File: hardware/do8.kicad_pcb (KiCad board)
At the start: 4 copper layers, 100 x 85 mm, 116 parts, among them J101 TNG-Power-TOP, J102 TNG-Power-BTM, J103 TNG-Data-TOP, J104 TNG-Data-BTM, P102 Debug, P103 PE, P201 OUTPUT0, P202 OUTPUT1, P203 OUTPUT2, P204 OUTPUT3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

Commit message: change value
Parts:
- C208: value 2.2uF/50V -> 4.7uF/50V

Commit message: specify tbd
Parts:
- C115: value TBD -> 2.2uF
- C127, C128: value 4.7nF/2kV -> 1nF/2kV
- R101: value 510 -> 1k
- RP201: value 200 -> 180
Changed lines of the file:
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@@
   (page A4)
   (layers
-    (0 F.Cu signal)
+    (0 F.Cu signal hide)
     (1 GND power hide)
     (2 VCC power hide)
@@
     (aux_axis_origin 89.8 62.5)
     (grid_origin 89.8 62.5)
-    (visible_elements FFFFFF7F)
+    (visible_elements FFFF7F7F)
     (pcbplotparams
       (layerselection 0x010fc_ffffffff)
@@
       (effects (font (size 0.29972 0.29972) (thickness 0.07493)))
     )
-    (fp_text value 200 (at 1.01 -0.02 90) (layer F.Fab)
+    (fp_text value 180 (at 1.01 -0.02 90) (layer F.Fab)
       (effects (font (size 0.29972 0.29972) (thickness 0.07493)))
     )
@@
       (effects (font (size 0.2 0.2) (thickness 0.05)) (justify mirror))
     )
-    (fp_text value TBD (at 0.05 0.375 180) (layer B.Fab)
+    (fp_text value 2.2uF (at 0.05 0.375 180) (layer B.Fab)
       (effects (font (size 0.2 0.2) (thickness 0.05)) (justify mirror))
     )
@@
       (effects (font (size 0.2 0.2) (thickness 0.05)))
     )
-    (fp_text value 510 (at 0 -0.15 90) (layer F.Fab)
+    (fp_text value 1k (at 0 -0.15 90) (layer F.Fab)
       (effects (font (size 0.2 0.2) (thickness 0.05)))
     )
@@
       (effects (font (size 0.3 0.3) (thickness 0.075)))
     )
-    (fp_text value 4.7nF/2kV (at 0 -0.65) (layer F.Fab)
+    (fp_text value 1nF/2kV (at 0 -0.65) (layer F.Fab)
       (effects (font (size 0.3 0.3) (thickness 0.075)))
     )
@@
       (effects (font (size 0.3 0.3) (thickness 0.075)))
     )
-    (fp_text value 4.7nF/2kV (at 0 -0.65) (layer F.Fab)
+    (fp_text value 1nF/2kV (at 0 -0.65) (layer F.Fab)
       (effects (font (size 0.3 0.3) (thickness 0.075)))
     )

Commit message: fix diodes
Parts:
- D201, D202, D203, D204, D205, D206, D207, D208: value SMBJ24A -> SMBJ24CA
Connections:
- J101 pad 21: (no net) -> Net-(J101-Pad21)
- J101 pad 22: (no net) -> Net-(J101-Pad22)
- J101 pad 23: (no net) -> Net-(J101-Pad23)
- J101 pad 24: (no net) -> Net-(J101-Pad24)
- J101 pad 25: (no net) -> Net-(J101-Pad25)
- J101 pad 26: (no net) -> Net-(J101-Pad26)
- J101 pad 27: (no net) -> Net-(J101-Pad27)
- J101 pad 28: (no net) -> Net-(J101-Pad28)
- J101 pad 29: (no net) -> Net-(J101-Pad29)
- J101 pad 30: (no net) -> Net-(J101-Pad30)
- J102 pad 21: (no net) -> Net-(J102-Pad21)
- J102 pad 22: (no net) -> Net-(J102-Pad22)
- J102 pad 23: (no net) -> Net-(J102-Pad23)
- J102 pad 24: (no net) -> Net-(J102-Pad24)
- J102 pad 25: (no net) -> Net-(J102-Pad25)
- J102 pad 26: (no net) -> Net-(J102-Pad26)
- J102 pad 27: (no net) -> Net-(J102-Pad27)
- J102 pad 28: (no net) -> Net-(J102-Pad28)
- J102 pad 29: (no net) -> Net-(J102-Pad29)
- J102 pad 30: (no net) -> Net-(J102-Pad30)
- J103 pad 35: (no net) -> Net-(J103-Pad35)
- J103 pad 37: (no net) -> Net-(J103-Pad37)
- U101 pad 11: (no net) -> Net-(U101-Pad11)
- U101 pad 17: (no net) -> Net-(U101-Pad17)
- U101 pad 2: (no net) -> Net-(U101-Pad2)
- U101 pad 21: (no net) -> Net-(U101-Pad21)
- U101 pad 22: (no net) -> Net-(U101-Pad22)
- U101 pad 26: (no net) -> Net-(U101-Pad26)
- U101 pad 27: (no net) -> Net-(U101-Pad27)
- U101 pad 28: (no net) -> Net-(U101-Pad28)
- U101 pad 3: (no net) -> Net-(U101-Pad3)
- U101 pad 4: (no net) -> Net-(U101-Pad4)
- U101 pad 43: (no net) -> Net-(U101-Pad43)
- U101 pad 46: (no net) -> Net-(U101-Pad46)
- U101 pad 7: (no net) -> Net-(U101-Pad7)
- U104 pad 7: (no net) -> Net-(U104-Pad7)
- U104 pad 8: (no net) -> Net-(U104-Pad8)
- U106 pad 12: (no net) -> Net-(U106-Pad12)
- U106 pad 2: (no net) -> Net-(U106-Pad2)
- U201 pad 2: (no net) -> Net-(U201-Pad2)
- U201 pad 26: (no net) -> Net-(U201-Pad26)
- U201 pad 27: (no net) -> Net-(U201-Pad27)
- U201 pad 28: (no net) -> Net-(U201-Pad28)
- U201 pad 29: (no net) -> Net-(U201-Pad29)
- U201 pad 30: (no net) -> Net-(U201-Pad30)

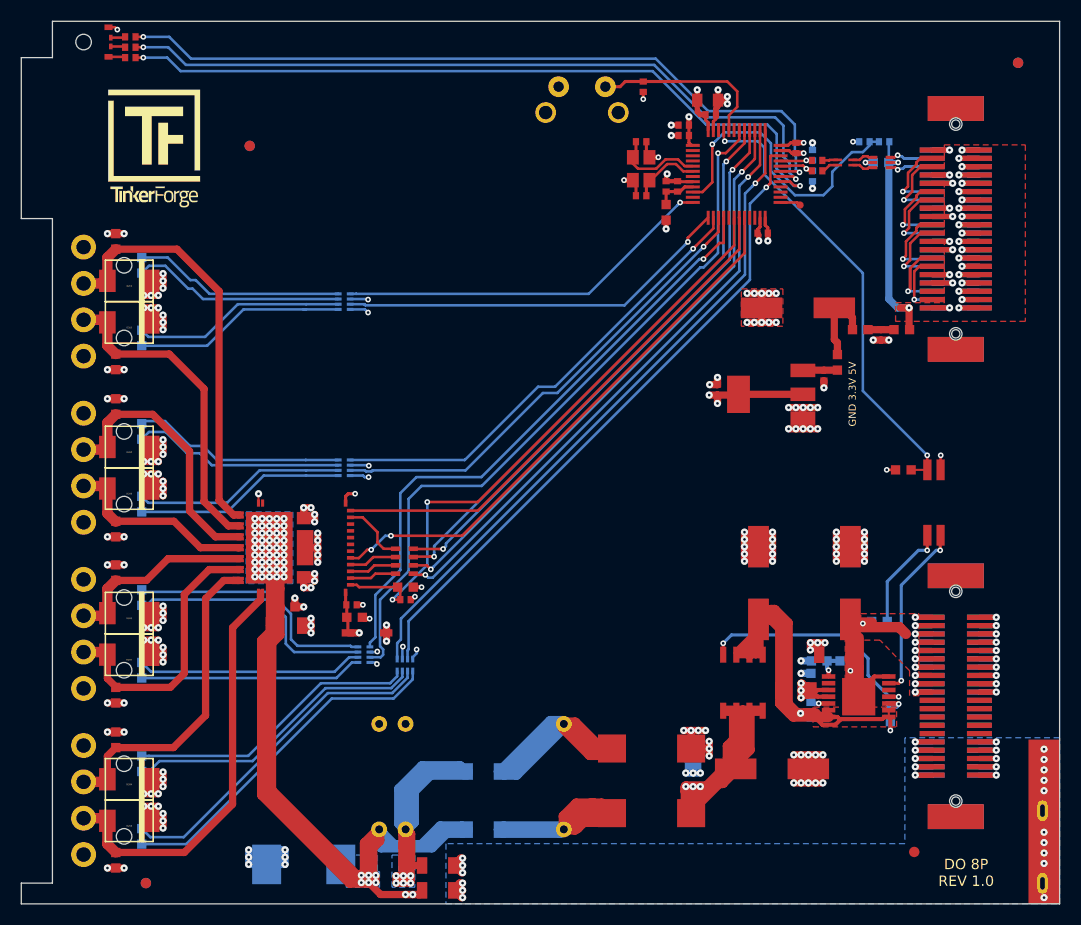
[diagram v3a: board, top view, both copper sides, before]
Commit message: version 1.1.
fix footprints
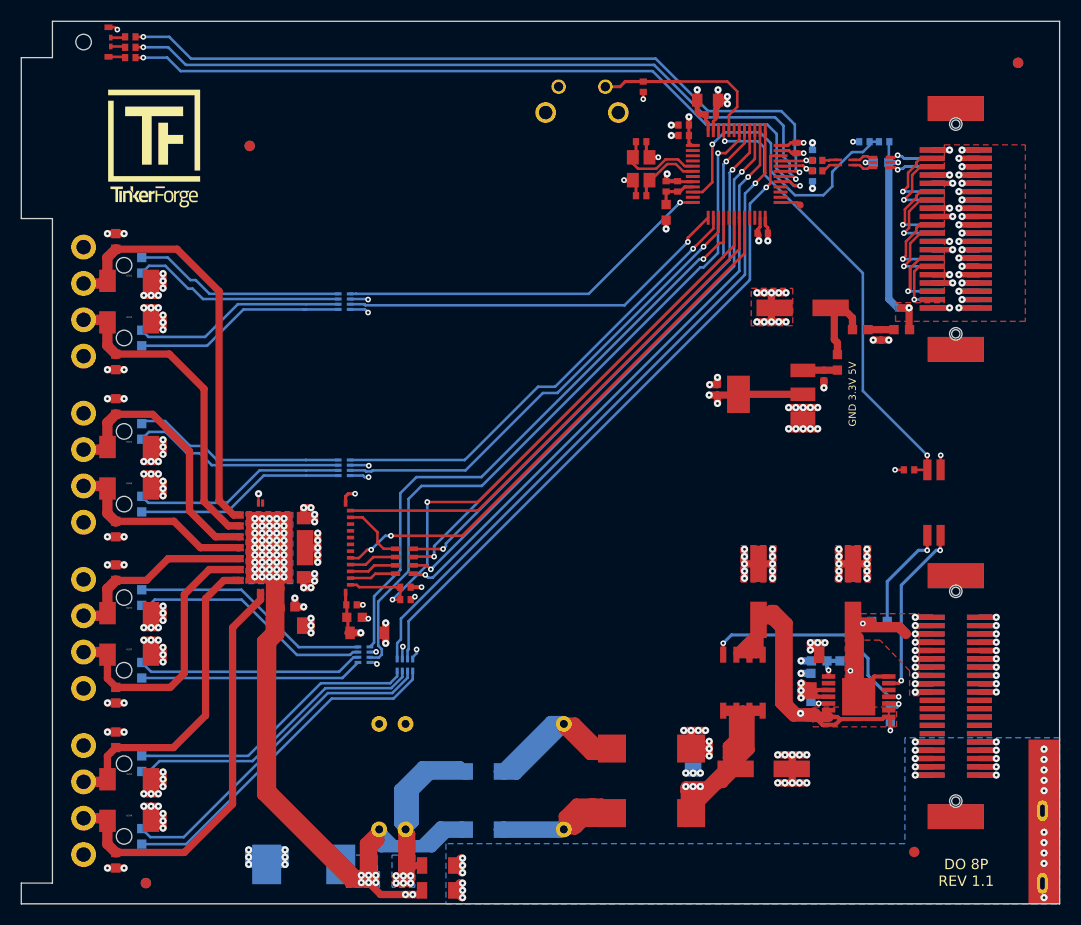
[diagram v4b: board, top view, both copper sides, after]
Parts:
- C108, C109: value TBD -> 33pF
- C111: value TBD -> 100µF; footprint kicad-libraries:ELKO_83 -> kicad-libraries:ELKO_63
- C121: value 10µF/35V -> 10µF/50V
- C122, C123, C124: footprint kicad-libraries:ELKO_83 -> kicad-libraries:ELKO_63
- D209: footprint kicad-libraries:SOD-123 -> kicad-libraries:SOD-123FL
- R109, R201: footprint kicad-libraries:R0603F -> kicad-libraries:R0402F
- X101: value TBD -> 3MHz
- moved C122 0.89 mm to (169.9, 117.5)
- moved C124 0.85 mm to (160.8, 117.5)
- moved C123 0.80 mm to (161.3, 134.5)
- moved R109 0.55 mm to (175.3, 105.7)
- moved C111 0.45 mm to (165.1, 90.1)
- turned D201 to 180 degrees
- turned D202 to 180 degrees
- turned D203 to 180 degrees
- turned D204 to 180 degrees
- turned D205 to 180 degrees
- turned D206 to 180 degrees
- turned D207 to 180 degrees
- turned D208 to 180 degrees
- turned D209 to 0 degrees
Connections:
- D201 pad 1: Net-(C211-Pad2) -> AGND
- D201 pad 2: AGND -> Net-(C211-Pad2)
- D202 pad 1: Net-(C207-Pad2) -> AGND
- D202 pad 2: AGND -> Net-(C207-Pad2)
- D203 pad 1: Net-(C205-Pad2) -> AGND
- D203 pad 2: AGND -> Net-(C205-Pad2)
- D204 pad 1: Net-(C203-Pad2) -> AGND
- D204 pad 2: AGND -> Net-(C203-Pad2)
- D205 pad 1: Net-(C209-Pad2) -> AGND
- D205 pad 2: AGND -> Net-(C209-Pad2)
- D206 pad 1: Net-(C206-Pad2) -> AGND
- D206 pad 2: AGND -> Net-(C206-Pad2)
- D207 pad 1: Net-(C204-Pad2) -> AGND
- D207 pad 2: AGND -> Net-(C204-Pad2)
- D208 pad 1: Net-(C202-Pad2) -> AGND
- D208 pad 2: AGND -> Net-(C202-Pad2)
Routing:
- net Net-(D214-Pad2): track 24.6 -> 23.2 mm
- net Net-(D214-Pad1): track 24.7 -> 23.4 mm
- added copper zone on F.Cu, net AGNDA
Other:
- board text added: "Copyright Tinkerforge GmbH 2020. This documentation describes Open Hardware and is licensed under the CERN OHL v. 1.1. You may redistribute and modify this documentation under the terms of the CERN OHL v.1.1. (http://ohwr.org/cernohl). This documentation is distributed WITHOUT ANY EXPRESS OR IMPLIED WARRANTY, INCLUDING OF MERCHANTABILITY, SATISFACTORY QUALITY AND FITNESS FOR A PARTICULAR PURPOSE.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"
- board text added: "DO 8P REV 1.1"
- board text removed: "DO 8P REV 1.0"

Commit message: fix values
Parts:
- C113, C114: value TBD/47pF -> 47pF
- X101: value 3MHz -> 8MHz

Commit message: fix footprint
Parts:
- C110: footprint C0805 -> kicad-libraries:C0805E

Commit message: fix values
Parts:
- C111: value 100µF -> 100uF
- C118, C121: value 10µF/50V -> 10uF/50V
- C122, C123, C124: value 100µF/35V -> 100uF/35V
- C125, C126: value 10µF/35V -> 10uF/35V
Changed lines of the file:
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@@
       (effects (font (size 0.3 0.3) (thickness 0.075)))
     )
-    (fp_text value 10µF/50V (at 0 -0.65 -180) (layer F.Fab)
+    (fp_text value 10uF/50V (at 0 -0.65 -180) (layer F.Fab)
       (effects (font (size 0.3 0.3) (thickness 0.075)))
     )
@@
       (effects (font (size 0.3 0.3) (thickness 0.075)) (justify mirror))
     )
-    (fp_text value 10µF/50V (at 0 0.65 90) (layer B.Fab)
+    (fp_text value 10uF/50V (at 0 0.65 90) (layer B.Fab)
       (effects (font (size 0.3 0.3) (thickness 0.075)) (justify mirror))
     )
@@
       (effects (font (size 0.3 0.3) (thickness 0.075)))
     )
-    (fp_text value 10µF/35V (at 0 -0.65) (layer F.Fab)
+    (fp_text value 10uF/35V (at 0 -0.65) (layer F.Fab)
       (effects (font (size 0.3 0.3) (thickness 0.075)))
     )
@@
       (effects (font (size 0.3 0.3) (thickness 0.075)))
     )
-    (fp_text value 10µF/35V (at 0 -0.65) (layer F.Fab)
+    (fp_text value 10uF/35V (at 0 -0.65) (layer F.Fab)
       (effects (font (size 0.3 0.3) (thickness 0.075)))
     )
@@
       (effects (font (size 0.59944 0.59944) (thickness 0.12446)))
     )
-    (fp_text value 100µF (at 0.95 -0.375) (layer F.Fab)
+    (fp_text value 100uF (at 0.95 -0.375) (layer F.Fab)
       (effects (font (size 0.59944 0.59944) (thickness 0.12446)))
     )
@@
       (effects (font (size 0.59944 0.59944) (thickness 0.12446)))
     )
-    (fp_text value 100µF/35V (at 0.95 -0.375 90) (layer F.Fab)
+    (fp_text value 100uF/35V (at 0.95 -0.375 90) (layer F.Fab)
       (effects (font (size 0.59944 0.59944) (thickness 0.12446)))
     )
@@
       (effects (font (size 0.59944 0.59944) (thickness 0.12446)))
     )
-    (fp_text value 100µF/35V (at 0.95 -0.375) (layer F.Fab)
+    (fp_text value 100uF/35V (at 0.95 -0.375) (layer F.Fab)
       (effects (font (size 0.59944 0.59944) (thickness 0.12446)))
     )
@@
       (effects (font (size 0.59944 0.59944) (thickness 0.12446)))
     )
-    (fp_text value 100µF/35V (at 0.95 -0.375 90) (layer F.Fab)
+    (fp_text value 100uF/35V (at 0.95 -0.375 90) (layer F.Fab)
       (effects (font (size 0.59944 0.59944) (thickness 0.12446)))
     )

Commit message: fix routing
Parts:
- C214: value 10pF -> 15pF
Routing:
- net LED5: track 70.4 -> 71.7 mm
